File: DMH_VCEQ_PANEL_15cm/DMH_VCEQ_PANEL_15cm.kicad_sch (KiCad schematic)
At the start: 9 parts, among them J0 Panel_GND_Solder_Wire_Pad

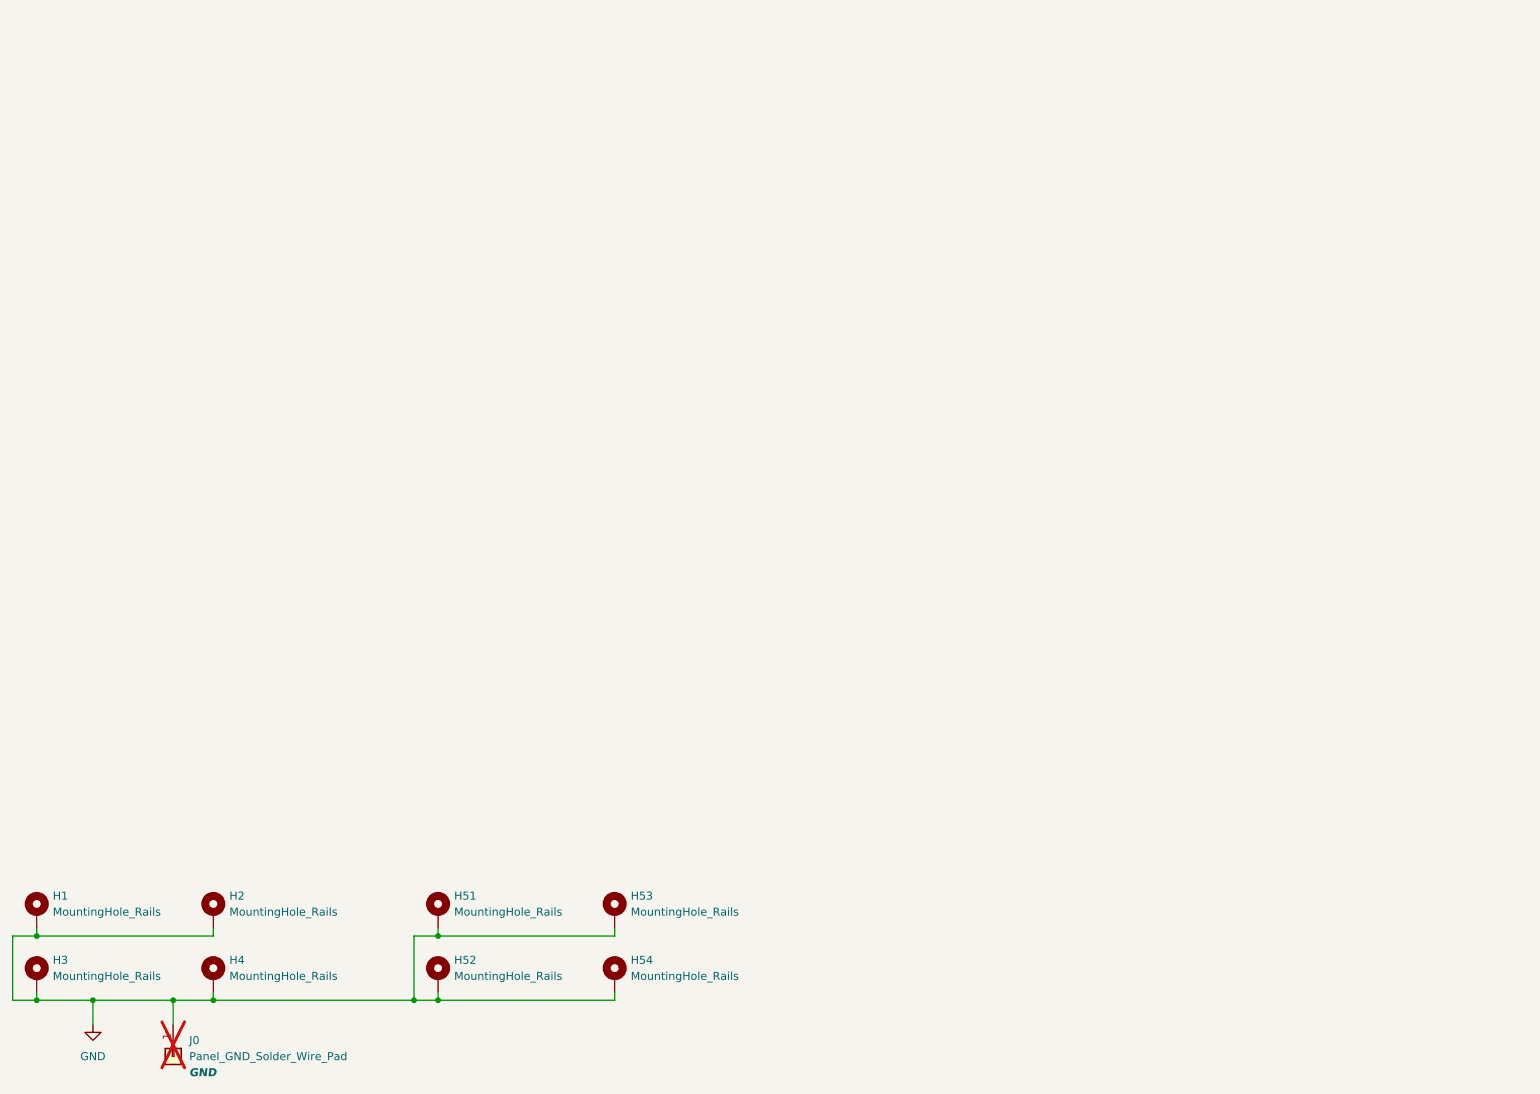
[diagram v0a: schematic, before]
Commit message: Designed 15cm panel version
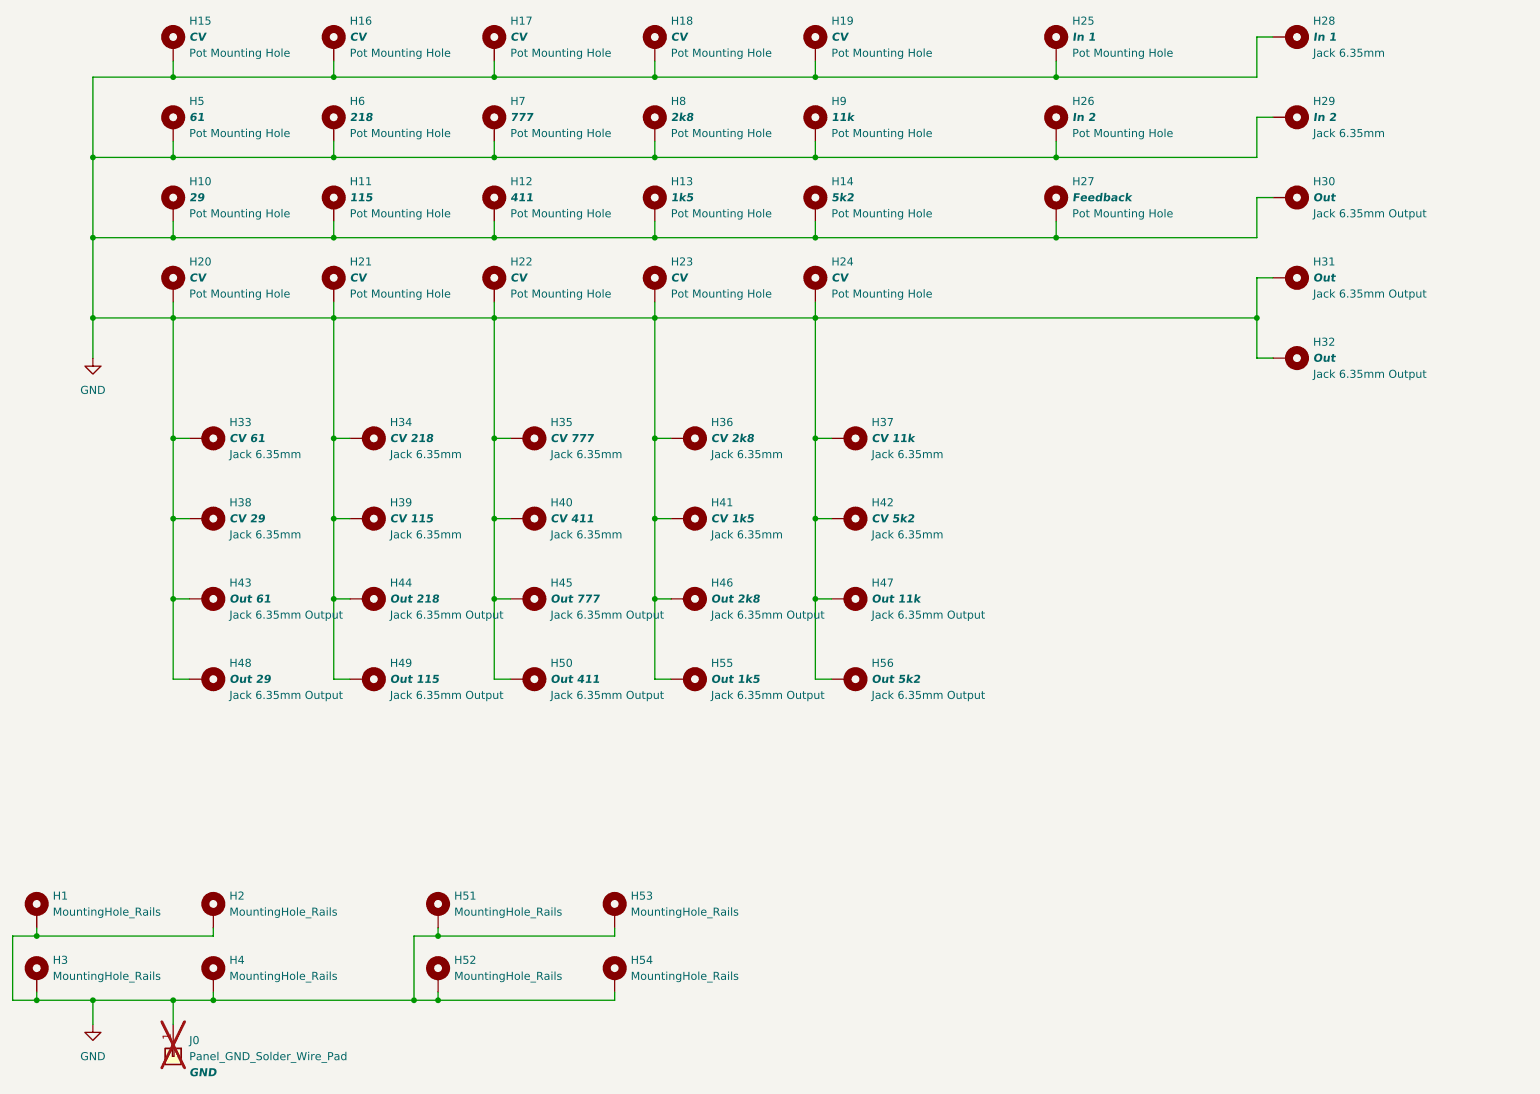
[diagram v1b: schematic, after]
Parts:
- added H10: 29, SynthStuff:Pot_Cutout_Small_attv_RD901F, symbol SynthStuff:MountingHole_Pot
- added H11: 115, SynthStuff:Pot_Cutout_Small_attv_RD901F, symbol SynthStuff:MountingHole_Pot
- added H12: 411, SynthStuff:Pot_Cutout_Small_attv_RD901F, symbol SynthStuff:MountingHole_Pot
- added H13: 1k5, SynthStuff:Pot_Cutout_Small_attv_RD901F, symbol SynthStuff:MountingHole_Pot
- added H14: 5k2, SynthStuff:Pot_Cutout_Small_attv_RD901F, symbol SynthStuff:MountingHole_Pot
- added H15, H16, H17, H18, H19, H20, H21, H22, H23, H24: CV, SynthStuff:Pot_Cutout_Tiny_attv_P110KH1, symbol SynthStuff:MountingHole_Pot
- added H25: In 1, SynthStuff:Pot_Cutout_Tiny, symbol SynthStuff:MountingHole_Pot
- added H26: In 2, SynthStuff:Pot_Cutout_Tiny, symbol SynthStuff:MountingHole_Pot
- added H27: Feedback, SynthStuff:Pot_Cutout_Tiny, symbol SynthStuff:MountingHole_Pot
- added H28: In 1, SynthStuff:Jack_6.35mm_Cutout_v3, symbol SynthStuff:MountingHole_Jack6.35mm_v2
- added H29: In 2, SynthStuff:Jack_6.35mm_Cutout_v3, symbol SynthStuff:MountingHole_Jack6.35mm_v2
- added H30, H31, H32: Out, SynthStuff:Jack_6.35mm_Cutout_Output_v6, symbol SynthStuff:MountingHole_Jack6.35mm_Output_v2
- added H33: CV 61, SynthStuff:Jack_6.35mm_Cutout_v3, symbol SynthStuff:MountingHole_Jack6.35mm_v2
- added H34: CV 218, SynthStuff:Jack_6.35mm_Cutout_v3, symbol SynthStuff:MountingHole_Jack6.35mm_v2
- added H35: CV 777, SynthStuff:Jack_6.35mm_Cutout_v3, symbol SynthStuff:MountingHole_Jack6.35mm_v2
- added H36: CV 2k8, SynthStuff:Jack_6.35mm_Cutout_v3, symbol SynthStuff:MountingHole_Jack6.35mm_v2
- added H37: CV 11k, SynthStuff:Jack_6.35mm_Cutout_v3, symbol SynthStuff:MountingHole_Jack6.35mm_v2
- added H38: CV 29, SynthStuff:Jack_6.35mm_Cutout_v3, symbol SynthStuff:MountingHole_Jack6.35mm_v2
- added H39: CV 115, SynthStuff:Jack_6.35mm_Cutout_v3, symbol SynthStuff:MountingHole_Jack6.35mm_v2
- added H40: CV 411, SynthStuff:Jack_6.35mm_Cutout_v3, symbol SynthStuff:MountingHole_Jack6.35mm_v2
- added H41: CV 1k5, SynthStuff:Jack_6.35mm_Cutout_v3, symbol SynthStuff:MountingHole_Jack6.35mm_v2
- added H42: CV 5k2, SynthStuff:Jack_6.35mm_Cutout_v3, symbol SynthStuff:MountingHole_Jack6.35mm_v2
- added H43: Out 61, SynthStuff:Jack_6.35mm_Cutout_Output_v6, symbol SynthStuff:MountingHole_Jack6.35mm_Output_v2
- added H44: Out 218, SynthStuff:Jack_6.35mm_Cutout_Output_v6, symbol SynthStuff:MountingHole_Jack6.35mm_Output_v2
- added H45: Out 777, SynthStuff:Jack_6.35mm_Cutout_Output_v6, symbol SynthStuff:MountingHole_Jack6.35mm_Output_v2
- added H46: Out 2k8, SynthStuff:Jack_6.35mm_Cutout_Output_v6, symbol SynthStuff:MountingHole_Jack6.35mm_Output_v2
- added H47: Out 11k, SynthStuff:Jack_6.35mm_Cutout_Output_v6, symbol SynthStuff:MountingHole_Jack6.35mm_Output_v2
- added H48: Out 29, SynthStuff:Jack_6.35mm_Cutout_Output_v6, symbol SynthStuff:MountingHole_Jack6.35mm_Output_v2
- added H49: Out 115, SynthStuff:Jack_6.35mm_Cutout_Output_v6, symbol SynthStuff:MountingHole_Jack6.35mm_Output_v2
- added H5: 61, SynthStuff:Pot_Cutout_Small_attv_RD901F, symbol SynthStuff:MountingHole_Pot
- added H50: Out 411, SynthStuff:Jack_6.35mm_Cutout_Output_v6, symbol SynthStuff:MountingHole_Jack6.35mm_Output_v2
- added H55: Out 1k5, SynthStuff:Jack_6.35mm_Cutout_Output_v6, symbol SynthStuff:MountingHole_Jack6.35mm_Output_v2
- added H56: Out 5k2, SynthStuff:Jack_6.35mm_Cutout_Output_v6, symbol SynthStuff:MountingHole_Jack6.35mm_Output_v2
- added H6: 218, SynthStuff:Pot_Cutout_Small_attv_RD901F, symbol SynthStuff:MountingHole_Pot
- added H7: 777, SynthStuff:Pot_Cutout_Small_attv_RD901F, symbol SynthStuff:MountingHole_Pot
- added H8: 2k8, SynthStuff:Pot_Cutout_Small_attv_RD901F, symbol SynthStuff:MountingHole_Pot
- added H9: 11k, SynthStuff:Pot_Cutout_Small_attv_RD901F, symbol SynthStuff:MountingHole_Pot
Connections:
- net GND: now also H10.1, H11.1, H12.1, H13.1, H14.1, H15.1, H16.1, H17.1, H18.1, H19.1, H20.1, H21.1, H22.1, H23.1, H24.1, H25.1, H26.1, H27.1, H28.1, H29.1, H30.1, H31.1, H32.1, H33.1, H34.1, H35.1, H36.1, H37.1, H38.1, H39.1, H40.1, H41.1, H42.1, H43.1, H44.1, H45.1, H46.1, H47.1, H48.1, H49.1, H5.1, H50.1, H55.1, H56.1, H6.1, H7.1, H8.1, H9.1

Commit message: Added FB/DW and M/S features
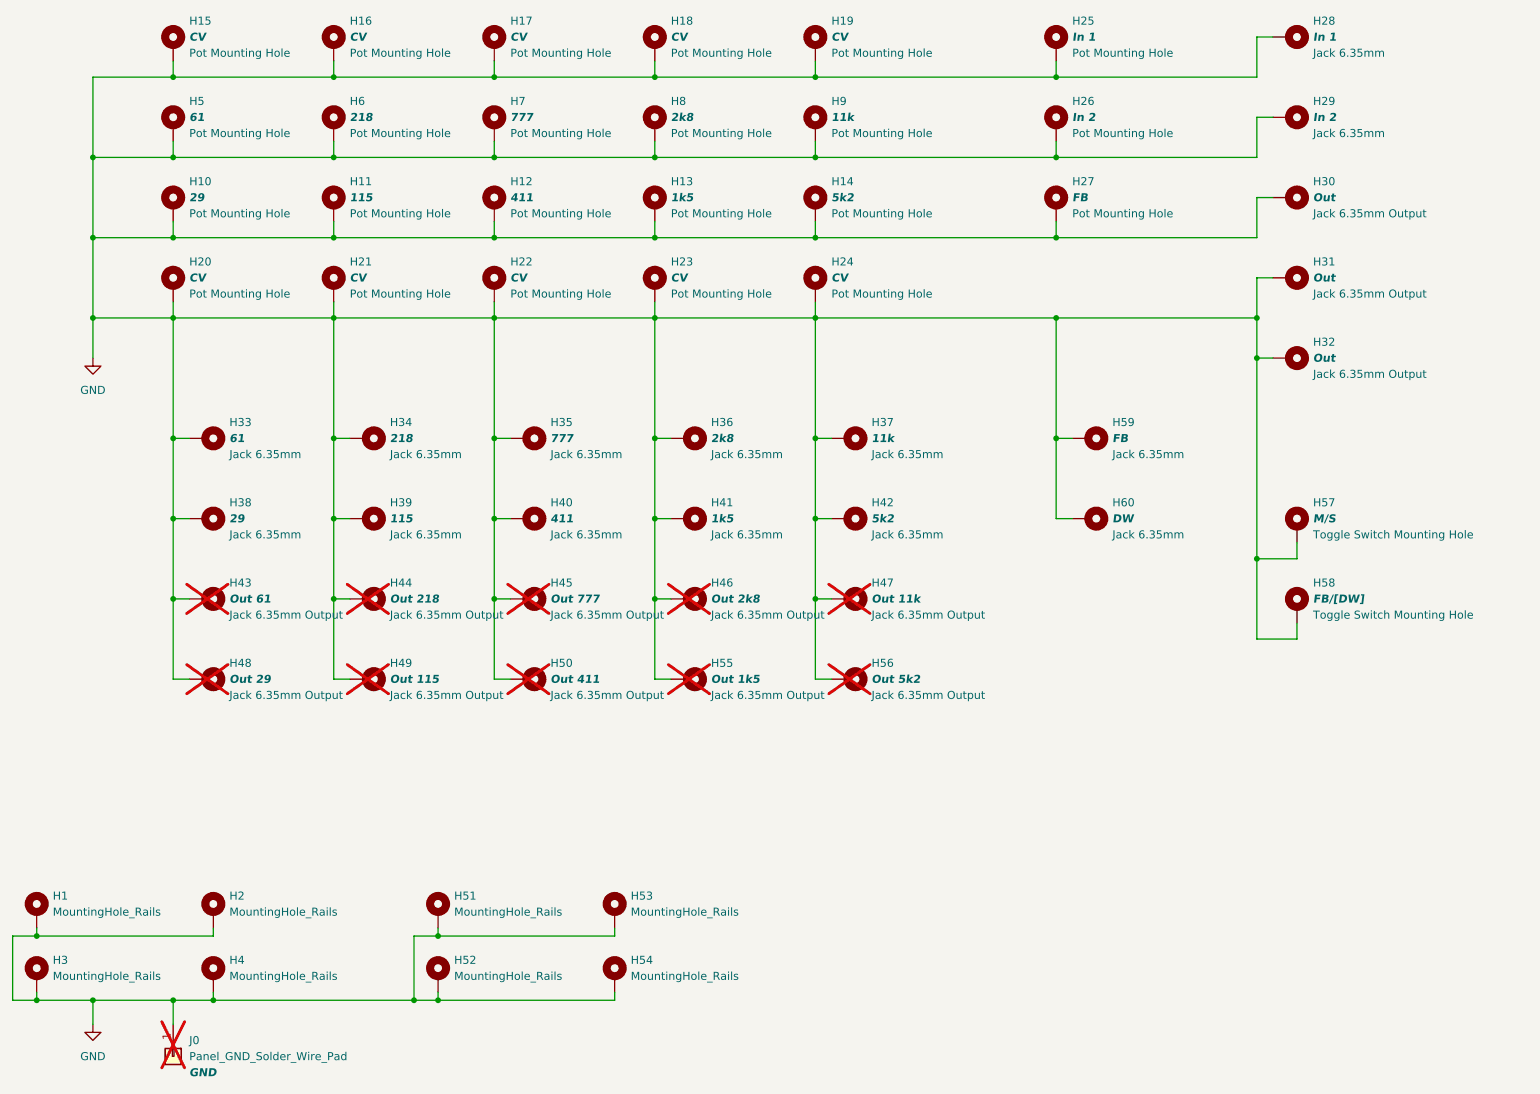
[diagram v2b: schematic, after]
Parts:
- added H57: M/S, SynthStuff:Toggle_Switch_TE_Cutout, symbol SynthStuff:MountingHole_ToggleSwitch
- added H58: FB/[DW], SynthStuff:Toggle_Switch_TE_Cutout, symbol SynthStuff:MountingHole_ToggleSwitch
- added H59: FB, SynthStuff:Jack_6.35mm_Cutout_v3, symbol SynthStuff:MountingHole_Jack6.35mm_v2
- added H60: DW, SynthStuff:Jack_6.35mm_Cutout_v3, symbol SynthStuff:MountingHole_Jack6.35mm_v2
- H27: value Feedback -> FB
- H33: value CV 61 -> 61
- H34: value CV 218 -> 218
- H35: value CV 777 -> 777
- H36: value CV 2k8 -> 2k8
- H37: value CV 11k -> 11k
- H38: value CV 29 -> 29
- H39: value CV 115 -> 115
- H40: value CV 411 -> 411
- H41: value CV 1k5 -> 1k5
- H42: value CV 5k2 -> 5k2
- H43, H44, H45, H46, H47, H48, H49, H50, H55, H56: now not fitted
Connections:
- net GND: now also H57.1, H58.1, H59.1, H60.1
